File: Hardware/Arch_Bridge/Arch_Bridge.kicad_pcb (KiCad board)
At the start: 2 copper layers, 88.8 x 76 mm, 97 parts, among them J1 Conn_01x02, J3 Conn_01x04, J4 Conn_01x04, Q1 2N3904, Q2 MJE2955, Q3 MJE2955, U1 AP63205WU, U10 74LVC1G04, U11 ESP32-S3-WROOM-1, U12 TXS0102DCT, U13 DRV8231ADDAR, U14 74LVC1G3208, U15 74LVC1G3208, U16 74LVC1G04, U17 TXS0102DCT, U18 TXS0102DCT, U19 TXS0108EPW, U2 NCP1117-3.3_SOT223, U20 TXS0108EPW, U3 LM393B, U4 74LVC1G04, U5 74LVC1G02, U6 TLP2770, U7 DRV8231ADDAR, U8 74LVC1G3208, U9 74LVC1G3208

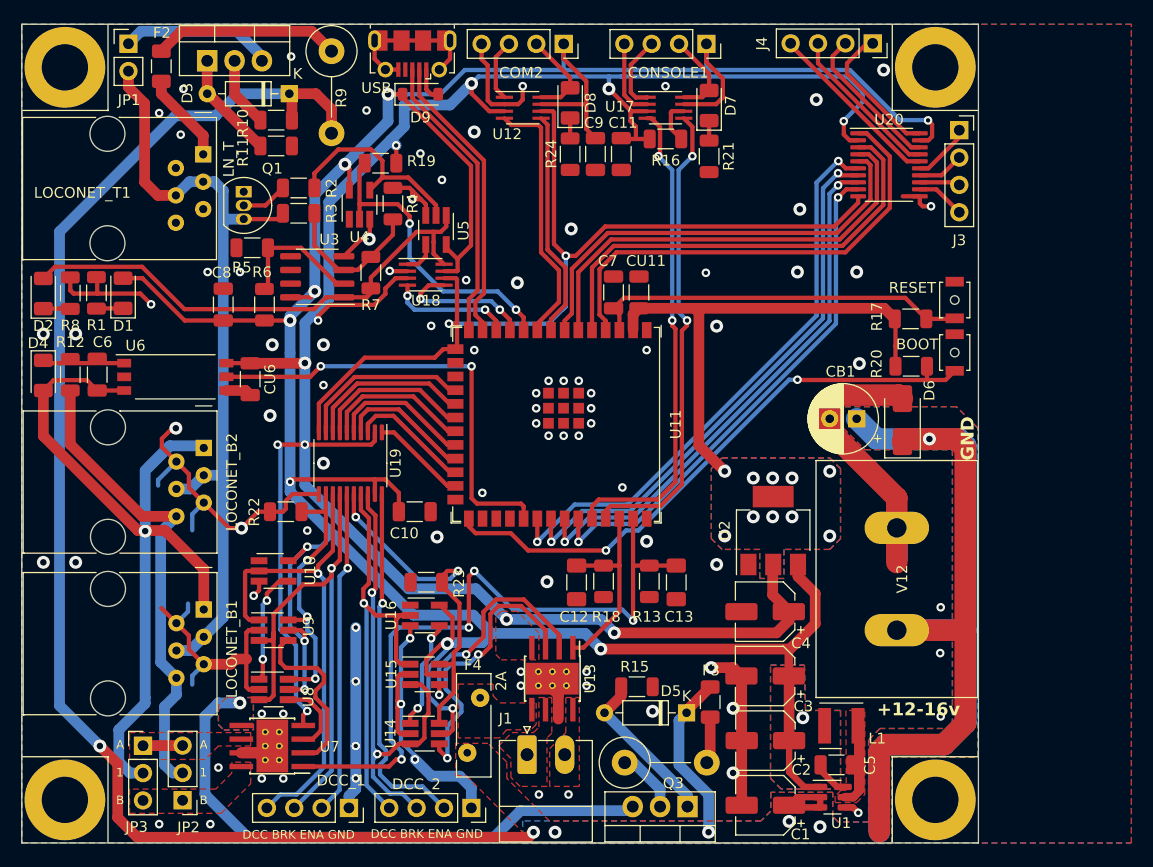
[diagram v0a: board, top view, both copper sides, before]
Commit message: Revised VIN to 5v power supply for better performance and less PCB space
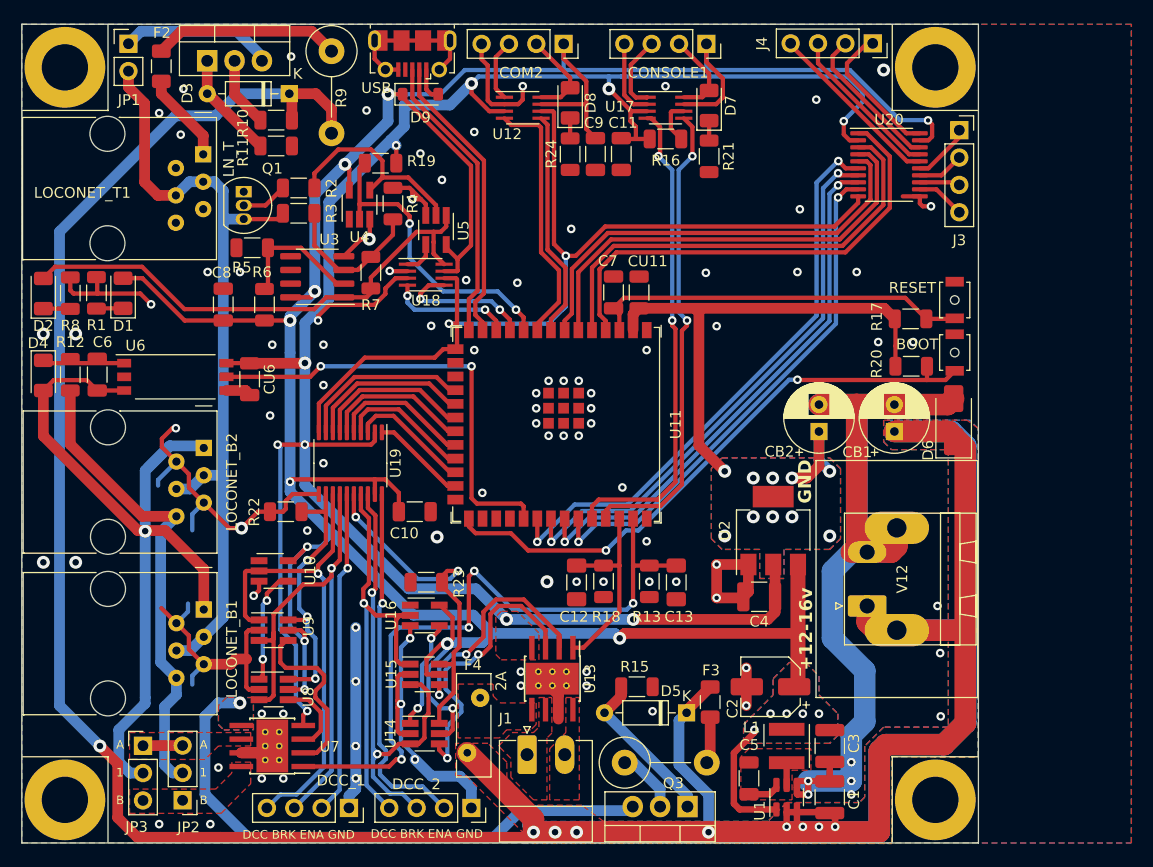
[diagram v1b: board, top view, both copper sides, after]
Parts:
- added CB2: 100uF, Capacitor_THT:CP_Radial_D6.3mm_P2.50mm, F.Cu at (94.0, 57.8)
- added V12A1: Conn_01x02, Connector_Phoenix_MSTB:PhoenixContact_MSTBA_2,5_2-G_1x02_P5.00mm_Horizontal, F.Cu at (98.5, 74.0)
- C1, C3, C4: value 22uF -> 10uF; footprint Capacitor_SMD:CP_Elec_5x5.3 -> Capacitor_SMD:C_1210_3225Metric
- CU11: value 0.1uf -> 0.1uF
- moved C3 8.85 mm to (95.0, 87.0), turned to -90 degrees
- moved C5 8.22 mm to (87.5, 90.0), turned to 90 degrees
- moved C1 6.02 mm to (95.0, 91.8), turned to 90 degrees
- moved L1 5.41 mm to (91.0, 87.0), turned to 90 degrees
- moved C2 5.02 mm to (89.5, 81.5)
- moved D6 4.75 mm to (106.5, 56.8)
- moved U1 4.25 mm to (91.0, 91.8), turned to 90 degrees
- moved CB1 3.69 mm to (101.0, 57.8), turned to 90 degrees
- moved C4 1.49 mm to (88.5, 73.2)
- moved CU6 0.05 mm to (41.1, 53.0)
- turned CU11 to -90 degrees
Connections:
- CU11 pad 1: +3.3V -> GND
- CU11 pad 2: GND -> +3.3V
- U11 pad 17: /GPIO9 -> unconnected-(U11-GPIO9/TOUCH9/ADC1_CH8/FSPIHD/SUBSPIHD-Pad17)
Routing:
- net +12V: track 269.5 -> 355.2 mm, vias 7 -> 9
- net GND: track 222.7 -> 282.5 mm, vias 90 -> 97
- net +3.3V: track 266.9 -> 273.9 mm
- net Net-(U1-SW): track 7.55 -> 2.31 mm
- net /SNS_1: track 64.5 -> 62.7 mm
- net Net-(U1-BST): track 3.38 -> 2.80 mm
- net +5V: track 311.6 -> 311.1 mm, vias 13 -> 17

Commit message: Relocated aux output for better cooling
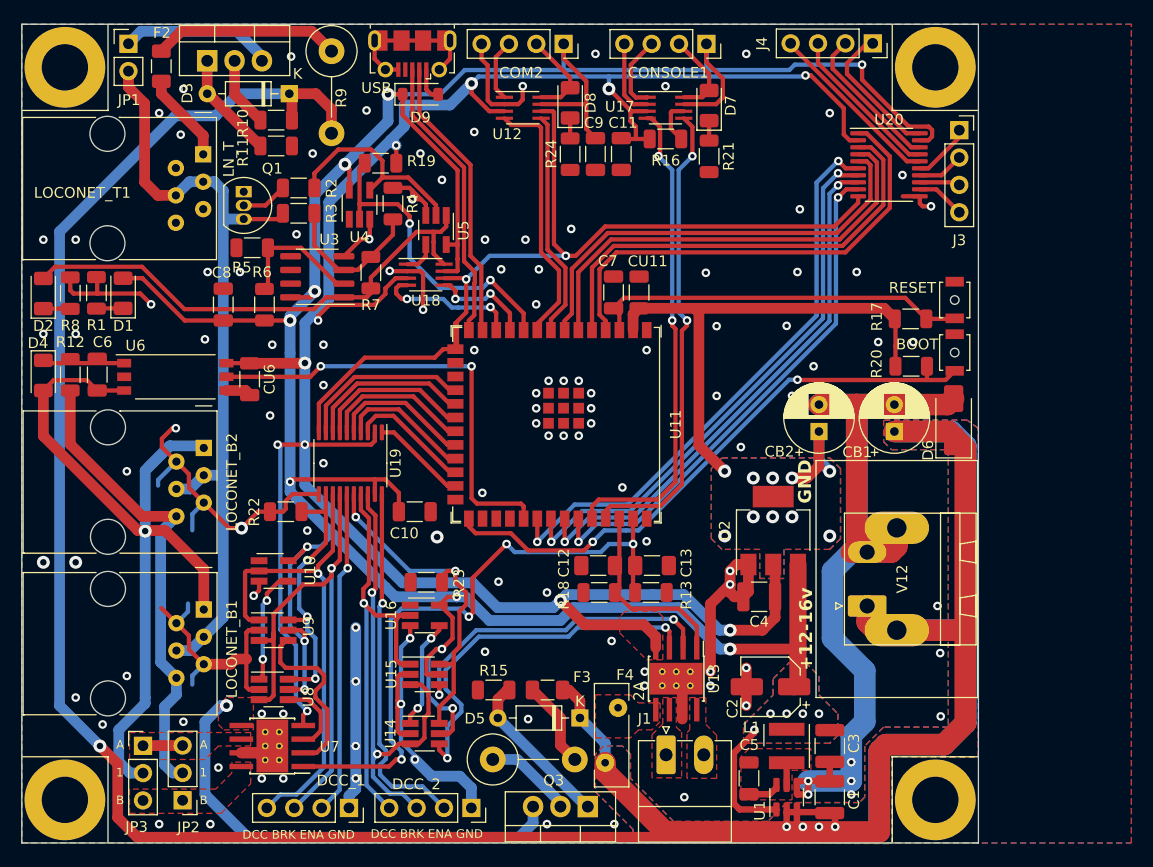
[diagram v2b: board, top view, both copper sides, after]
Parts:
- moved F3 15.1 mm to (68.8, 81.8), turned to 0 degrees
- moved R15 13.3 mm to (63.8, 81.8), turned to 0 degrees
- moved J1 12.9 mm to (79.8, 87.8)
- moved F4 12.8 mm to (74.2, 88.5)
- moved R14 12.3 mm to (63.7, 88.2)
- moved U13 11.5 mm to (80.8, 80.8)
- moved D5 9.91 mm to (71.8, 84.4)
- moved Q3 9.25 mm to (72.5, 92.6)
- moved C13 2.74 mm to (78.5, 70.2), turned to 0 degrees
- moved C12 2.54 mm to (73.5, 70.2), turned to 180 degrees
- moved R18 1.11 mm to (73.6, 72.8), turned to 0 degrees
- moved R13 1.05 mm to (78.4, 72.8), turned to 180 degrees
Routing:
- net +12V: track 355.2 -> 315.1 mm, vias 9 -> 5
- net +3.3V: track 273.9 -> 284.0 mm
- net Net-(Q3-E): track 53.6 -> 43.6 mm
- net GND: track 282.5 -> 292.2 mm, vias 97 -> 119
- net Net-(U13-IN2): track 21.2 -> 30.1 mm
- net Net-(U13-IN1): track 27.0 -> 35.0 mm
- net /SNS_1: track 62.7 -> 57.5 mm
- net Net-(F3-Pad1): track 4.35 -> 8.08 mm
- net /LN_RX: track 13.1 -> 9.62 mm
- net /OE: track 87.0 -> 83.8 mm
- net +5V: track 311.1 -> 308.5 mm, vias 17 -> 18
- net Net-(Q3-C): track 5.93 -> 8.32 mm
- net /LN_COLL: track 11.4 -> 13.3 mm
- net /LN_TX: track 28.5 -> 29.3 mm
- net /USB_D-: track 27.3 -> 26.6 mm
- removed copper zone on B.Cu, net Net-(Q3-E)

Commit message: R15 could overheat, changed R14 and R15 to 2512 package SMDs for 1w thermal and simplified assembly. PCB rev 11. Also debugging of Loconet TX delay and throttle/turnout commands
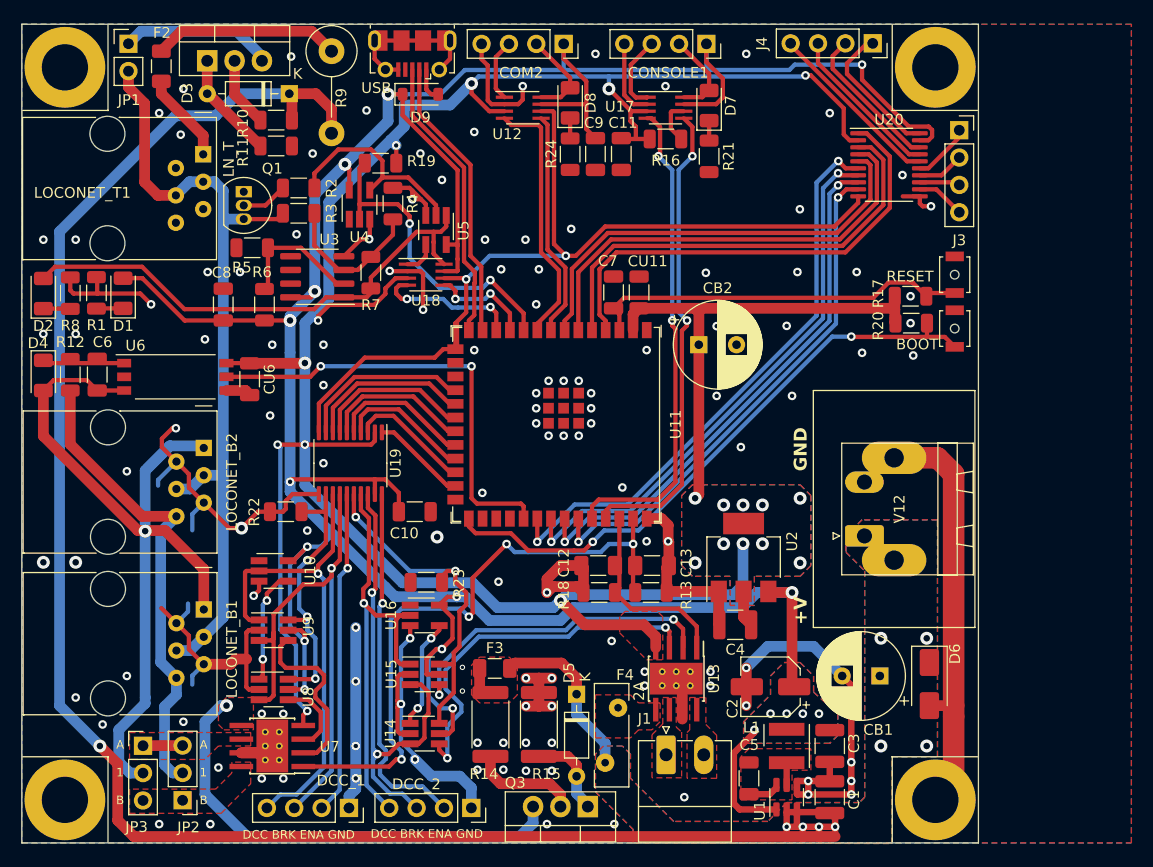
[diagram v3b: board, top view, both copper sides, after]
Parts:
- CB1, CB2: footprint Capacitor_THT:CP_Radial_D6.3mm_P2.50mm -> Capacitor_THT:CP_Radial_D8.0mm_P3.50mm
- D6: value SMAJ18CA -> SMAJ24CA
- D9: value PMEG2005EGW -> PMEG2005EGWX
- R14: footprint Resistor_THT:R_Axial_DIN0414_L11.9mm_D4.5mm_P7.62mm_Vertical -> Resistor_SMD:R_2512_6332Metric
- R15: footprint Resistor_SMD:R_1206_3216Metric -> Resistor_SMD:R_2512_6332Metric
- U2: value NCP1117-3.3_SOT223 -> TLV1117LV33DCYR
- moved D6 24.6 mm to (104.2, 81.2), turned to -90 degrees
- moved CB1 22.7 mm to (99.7, 80.5), turned to 180 degrees
- moved CB2 13.8 mm to (82.8, 49.8), turned to 0 degrees
- moved V12 6.50 mm to (101.0, 65.0)
- moved V12A1 6.50 mm to (98.2, 67.5)
- moved F3 5.29 mm to (63.9, 79.8)
- moved R15 5.28 mm to (68.0, 85.0), turned to -90 degrees
- moved R20 4.00 mm to (102.6, 47.8)
- moved U2 3.72 mm to (87.0, 69.5)
- moved C4 3.42 mm to (86.2, 75.8)
- moved R14 3.26 mm to (63.5, 85.0), turned to 90 degrees
- moved RESET1 2.35 mm to (106.6, 43.2)
- moved D5 2.23 mm to (71.5, 82.2), turned to -90 degrees
- moved BOOT1 2.23 mm to (106.6, 48.2)
- moved R17 2.10 mm to (102.5, 45.2)
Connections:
- ? pad 1: (no net) -> GND
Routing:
- net +12V: track 315.1 -> 192.3 mm, vias 5 -> 9
- net +3.3V: track 284.0 -> 270.7 mm, vias 21 -> 20
- net Net-(D5-A): track 14.9 -> 7.92 mm
- net Net-(F3-Pad1): track 8.08 -> 2.20 mm
- net GND: track 292.2 -> 287.7 mm, vias 119 -> 128
- net +5V: track 308.5 -> 306.5 mm
- net Net-(Q3-C): track 8.32 -> 10.0 mm
- net Net-(U11-GPIO0/BOOT): track 55.0 -> 56.7 mm
- added copper zone on F.Cu, net Net-(F3-Pad1)
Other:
- board text added: "+V"
- board text removed: "+12-16v"

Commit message: Checkpoint
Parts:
- removed F3: 250mA, Fuse:Fuse_1206_3216Metric
- added D10: Z-12, Diode_SMD:D_MiniMELF, F.Cu at (35.5, 26.8)
- D3, D5: value 1N5231B -> Z-5.1; footprint Diode_THT:D_DO-35_SOD27_P7.62mm_Horizontal -> Diode_SMD:D_MiniMELF
- Q1: value 2N3904 -> MMBT3904; footprint Package_TO_SOT_THT:TO-92_Inline -> Package_TO_SOT_SMD:SOT-23
- Q2: value MJE2955 -> MMBT3906; footprint Package_TO_SOT_THT:TO-220-3_Vertical -> Package_TO_SOT_SMD:SOT-23
- R9: footprint Resistor_THT:R_Axial_DIN0414_L11.9mm_D4.5mm_P7.62mm_Vertical -> Resistor_THT:R_Axial_DIN0516_L15.5mm_D5.0mm_P5.08mm_Vertical
- moved D3 14.3 mm to (31.0, 22.8), turned to -90 degrees
- moved JP1 14.2 mm to (41.5, 30.0)
- moved F1 13.9 mm to (46.5, 27.0), turned to 0 degrees
- moved R11 13.9 mm to (30.5, 26.8)
- moved R10 8.73 mm to (37.0, 23.1), turned to -90 degrees
- moved D5 6.06 mm to (71.5, 88.2)
- moved Q2 3.21 mm to (34.0, 23.5), turned to 90 degrees
- moved R9 2.66 mm to (46.1, 23.0), turned to 180 degrees
- moved Q1 1.30 mm to (41.6, 36.4)
- moved R2 0.38 mm to (45.7, 35.6)
- moved R3 0.38 mm to (45.7, 37.9)
- renumbered F2 to F1, F4 to F2, V12A1 to V12, V12 to V12A1
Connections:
- JP1 pad 1: Net-(Q2-E) -> Net-(D10-K)
- Q1 pad 1: GND -> Net-(Q1-B)
- Q1 pad 2: Net-(Q1-B) -> GND
- Q2 pad 2: Net-(Q2-C) -> Net-(D10-K)
- Q2 pad 3: Net-(Q2-E) -> Net-(Q2-C)
- R14 pad 2: Net-(F3-Pad1) -> +12V
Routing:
- net Net-(Q2-E): track 14.2 -> 0.00 mm
- net Net-(F1-Pad2): track 17.3 -> 4.73 mm
- net Net-(D10-K): track 0.00 -> 10.3 mm
- net /LN_DAT: track 75.5 -> 66.5 mm, vias 0 -> 1
- net /T_PWR: track 8.39 -> 14.9 mm, vias 0 -> 1
- net Net-(D3-A): track 10.0 -> 5.78 mm
- net +12V: track 192.3 -> 195.3 mm
- net Net-(Q1-B): track 4.31 -> 1.74 mm
- net Net-(Q2-C): track 6.50 -> 4.29 mm
- net Net-(F3-Pad1): track 2.20 -> 0.00 mm
- net GND: vias 128 -> 129
- removed copper zone on F.Cu, net Net-(F3-Pad1)
